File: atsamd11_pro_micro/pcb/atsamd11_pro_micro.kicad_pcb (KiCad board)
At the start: 2 copper layers, 33 x 17.8 mm, 24 parts, among them U1 MCP1700T-3302E/MB

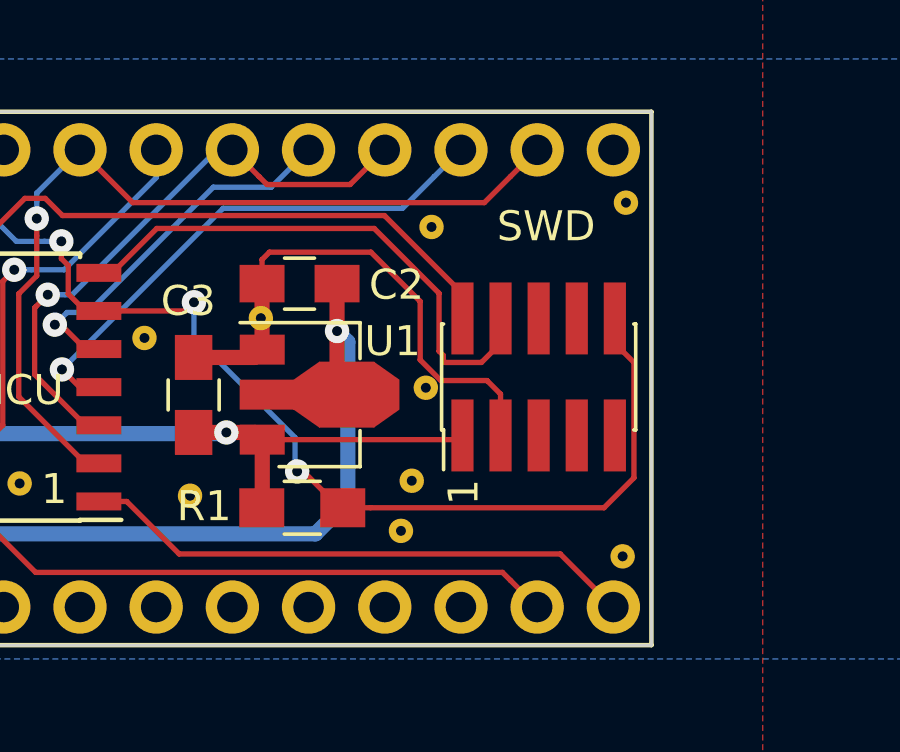
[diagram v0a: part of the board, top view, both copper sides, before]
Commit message: atsamd11_pro_micro: added missing SWCLK pullup
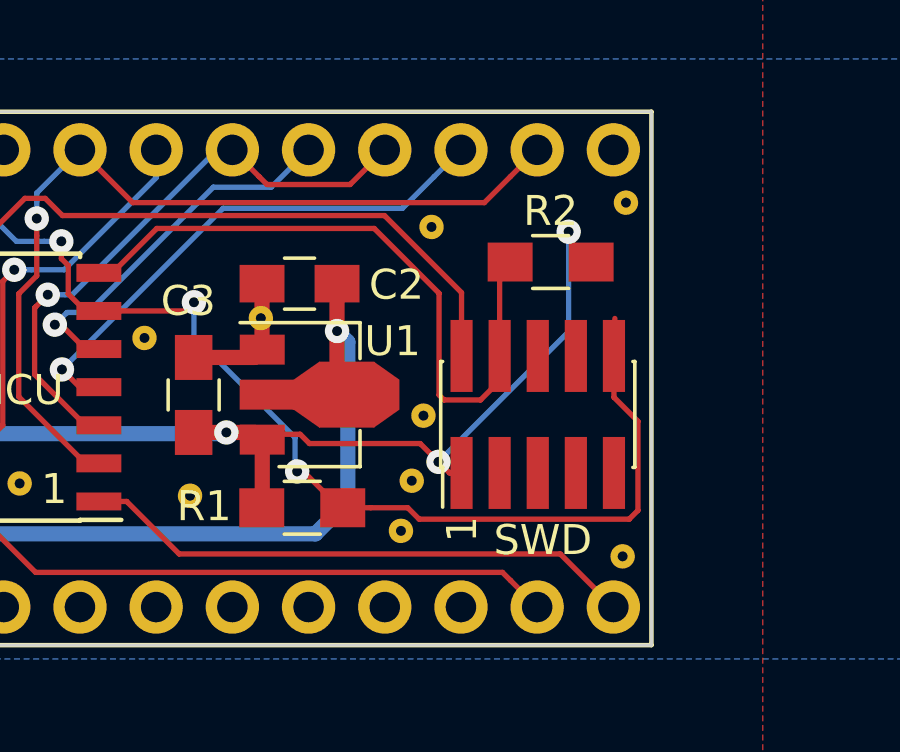
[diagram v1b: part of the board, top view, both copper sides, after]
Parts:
- added R2: 1k, Resistors_SMD:R_0805_HandSoldering, F.Cu at (157.9, 116.8)
- moved SWD 1.25 mm to (157.5, 121.8)
- moved staple_single15 0.93 mm to (153.7, 121.9)
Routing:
- net GND: track 23.5 -> 10.2 mm
- net 3V3: track 34.4 -> 45.7 mm, vias 2 -> 4
- net SWCLK: track 18.2 -> 22.7 mm
- net SWDIO: track 20.7 -> 21.9 mm
- net mcu_RESET: track 37.0 -> 37.7 mm
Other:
- board text added: "atsamd11 breakout board r2 Copyright 2017 Google Inc Designed by Phillip Pearson github.com/google/ myelin-acorn-electron-hardware"
- board text removed: "atsamd11 breakout board Copyright 2017 Google Inc Designed by Phillip Pearson github.com/google/ myelin-acorn-electron-hardware"

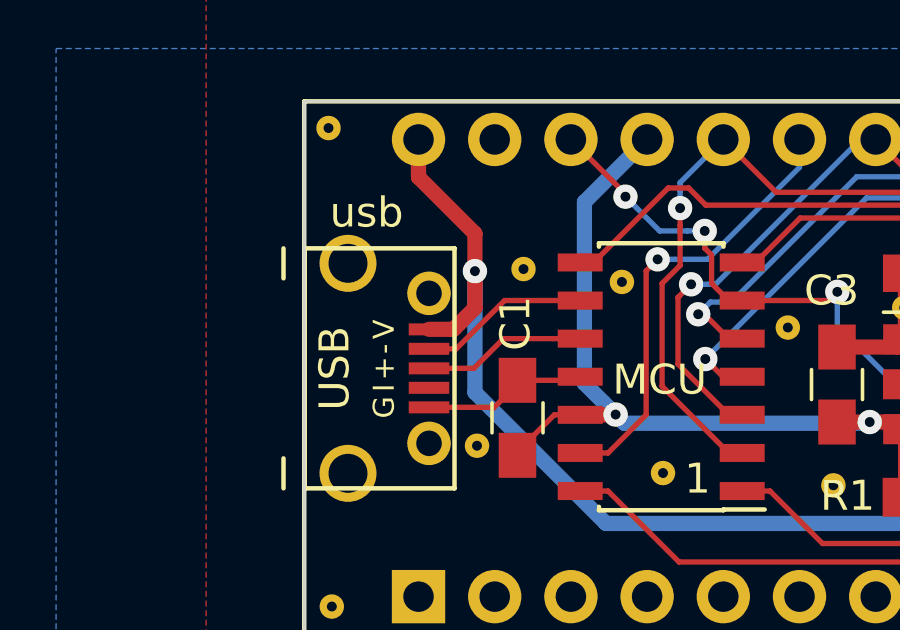
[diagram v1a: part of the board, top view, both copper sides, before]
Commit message: atsamd11_pro_micro tested out well
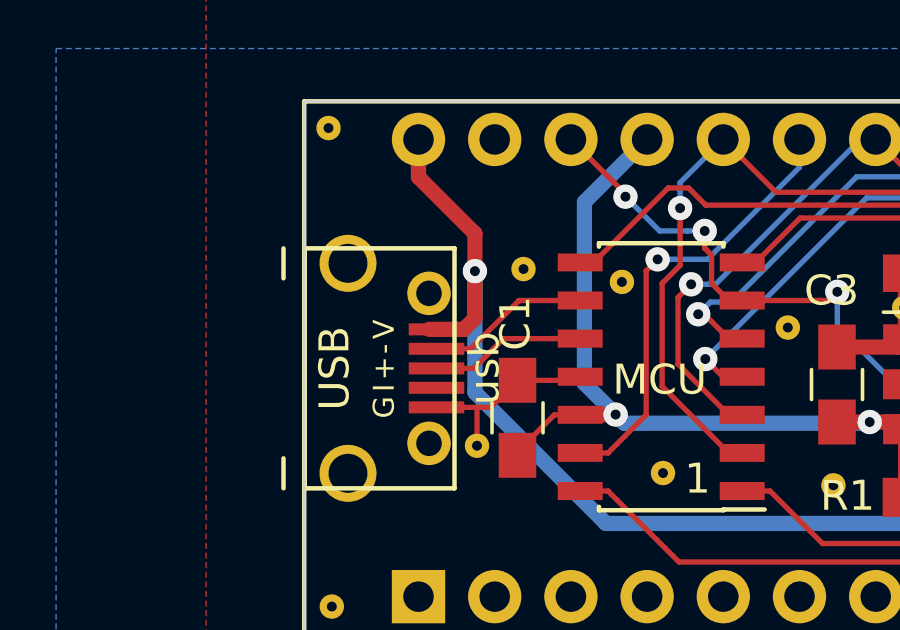
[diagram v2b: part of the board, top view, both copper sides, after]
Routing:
- net GND: track 10.2 -> 11.3 mm
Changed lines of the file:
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@@
     (links 56)
     (no_connects 0)
-    (area 128.219999 111.709999 161.340001 129.590001)
+    (area 120 105 170.000001 135.000001)
     (thickness 1.6)
     (drawings 7)
@@
     )
   )
-  (module myelin-kicad:micro_usb_b_smd_molex (layer F.Cu)
-    (at 130.28 120.66 270)
-    (descr "Molex SD-105017-001 bottom mount micro USB socket")
-    (fp_text reference USB (at 0 1 270) (layer F.SilkS)
-      (effects (font (size 1 1) (thickness 0.15)))
-    )
-    (fp_text value usb (at -5.19 -0.07 360) (layer F.SilkS)
-      (effects (font (size 1 1) (thickness 0.15)))
-    )
-    (fp_line (start -4 -3) (end 4 -3) (layer F.SilkS) (width 0.15))
-    (fp_line (start -4 -3) (end -4 2) (layer F.SilkS) (width 0.15))
-    (fp_line (start -4 2) (end 4 2) (layer F.SilkS) (width 0.15))
-    (fp_line (start 4 -3) (end 4 2) (layer F.SilkS) (width 0.15))
-    (fp_line (start -4 2.7) (end -3 2.7) (layer F.SilkS) (width 0.15))
-    (fp_line (start 3 2.7) (end 4 2.7) (layer F.SilkS) (width 0.15))
-    (fp_text user V (at -1.3 -0.65 270) (layer F.SilkS)
-      (effects (font (size 0.7 0.7) (thickness 0.15)))
-    )
-    (fp_text user - (at -0.65 -0.65 270) (layer F.SilkS)
-      (effects (font (size 0.7 0.7) (thickness 0.15)))
-    )
-    (fp_text user + (at 0 -0.65 270) (layer F.SilkS)
-      (effects (font (size 0.7 0.7) (thickness 0.15)))
-    )
-    (fp_text user I (at 0.65 -0.65 270) (layer F.SilkS)
-      (effects (font (size 0.7 0.7) (thickness 0.15)))
-    )
-    (fp_text user G (at 1.3 -0.65 270) (layer F.SilkS)
-      (effects (font (size 0.7 0.7) (thickness 0.15)))
-    )
-    (pad 1 smd rect (at -1.3 -2.15 270) (size 0.4 1.35) (layers F.Cu F.Paste F.Mask)
-      (net 2 5V))
-    (pad 2 smd rect (at -0.65 -2.15 270) (size 0.4 1.35) (layers F.Cu F.Paste F.Mask)
-      (net 12 USBDM))
-    (pad 3 smd rect (at 0 -2.15 270) (size 0.4 1.35) (layers F.Cu F.Paste F.Mask)
-      (net 13 USBDP))
-    (pad 4 smd rect (at 0.65 -2.15 270) (size 0.4 1.35) (layers F.Cu F.Paste F.Mask)
-      (net 18 USB_ID))
-    (pad 5 smd rect (at 1.3 -2.15 270) (size 0.4 1.35) (layers F.Cu F.Paste F.Mask)
-      (net 1 GND))
-    (pad P0 thru_hole circle (at -2.5 -2.15 270) (size 1.45 1.45) (drill 0.85) (layers *.Cu *.Mask))
-    (pad P1 thru_hole circle (at 2.5 -2.15 270) (size 1.45 1.45) (drill 0.85) (layers *.Cu *.Mask))
-    (pad M0 thru_hole circle (at -3.5 0.55 270) (size 1.9 1.9) (drill 1.3) (layers *.Cu *.Mask))
-    (pad M1 thru_hole circle (at 3.5 0.55 270) (size 1.9 1.9) (drill 1.3) (layers *.Cu *.Mask))
-  )
   (module myelin-kicad:via_single (layer F.Cu)
     (at 129.19 128.6)
@@
     )
   )
+  (module myelin-kicad:micro_usb_b_smd_molex (layer F.Cu)
+    (at 130.28 120.66 270)
+    (descr "Molex SD-105017-001 bottom mount micro USB socket")
+    (fp_text reference USB (at 0 1 270) (layer F.SilkS)
+      (effects (font (size 1 1) (thickness 0.15)))
+    )
+    (fp_text value usb (at 0 -4 270) (layer F.SilkS)
+      (effects (font (size 1 1) (thickness 0.15)))
+    )
+    (fp_line (start -4 -3) (end 4 -3) (layer F.SilkS) (width 0.15))
+    (fp_line (start -4 -3) (end -4 2) (layer F.SilkS) (width 0.15))
+    (fp_line (start -4 2) (end 4 2) (layer F.SilkS) (width 0.15))
+    (fp_line (start 4 -3) (end 4 2) (layer F.SilkS) (width 0.15))
+    (fp_line (start -4 2.7) (end -3 2.7) (layer F.SilkS) (width 0.15))
+    (fp_line (start 3 2.7) (end 4 2.7) (layer F.SilkS) (width 0.15))
+    (fp_text user V (at -1.3 -0.65 270) (layer F.SilkS)
+      (effects (font (size 0.7 0.7) (thickness 0.15)))
+    )
+    (fp_text user - (at -0.65 -0.65 270) (layer F.SilkS)
+      (effects (font (size 0.7 0.7) (thickness 0.15)))
+    )
+    (fp_text user + (at 0 -0.65 270) (layer F.SilkS)
+      (effects (font (size 0.7 0.7) (thickness 0.15)))
+    )
+    (fp_text user I (at 0.65 -0.65 270) (layer F.SilkS)
+      (effects (font (size 0.7 0.7) (thickness 0.15)))
+    )
+    (fp_text user G (at 1.3 -0.65 270) (layer F.SilkS)
+      (effects (font (size 0.7 0.7) (thickness 0.15)))
+    )
+    (pad 1 smd rect (at -1.3 -2.4 270) (size 0.4 1.85) (layers F.Cu F.Paste F.Mask)
+      (net 2 5V))
+    (pad 2 smd rect (at -0.65 -2.4 270) (size 0.4 1.85) (layers F.Cu F.Paste F.Mask)
+      (net 12 USBDM))
+    (pad 3 smd rect (at 0 -2.4 270) (size 0.4 1.85) (layers F.Cu F.Paste F.Mask)
+      (net 13 USBDP))
+    (pad 4 smd rect (at 0.65 -2.4 270) (size 0.4 1.85) (layers F.Cu F.Paste F.Mask)
+      (net 18 USB_ID))
+    (pad 5 smd rect (at 1.3 -2.4 270) (size 0.4 1.85) (layers F.Cu F.Paste F.Mask)
+      (net 1 GND))
+    (pad P0 thru_hole circle (at -2.5 -2.15 270) (size 1.45 1.45) (drill 0.85) (layers *.Cu *.Mask))
+    (pad P1 thru_hole circle (at 2.5 -2.15 270) (size 1.45 1.45) (drill 0.85) (layers *.Cu *.Mask))
+    (pad M0 thru_hole circle (at -3.5 0.55 270) (size 1.9 1.9) (drill 1.3) (layers *.Cu *.Mask))
+    (pad M1 thru_hole circle (at 3.5 0.55 270) (size 1.9 1.9) (drill 1.3) (layers *.Cu *.Mask))
+  )
   (gr_text 1 (at 154.98 125.68 90) (layer F.SilkS)
     (effects (font (size 1 1) (thickness 0.2)))
@@
   (gr_line (start 161.29 111.76) (end 161.29 129.54) (layer Edge.Cuts) (width 0.1))
   (gr_line (start 128.27 111.76) (end 161.29 111.76) (layer Edge.Cuts) (width 0.1))
+  (segment (start 132.43 121.96) (end 134.01 121.96) (width 0.1778) (layer F.Cu) (net 1))
+  (segment (start 134.01 121.96) (end 134.48 121.96) (width 0.1778) (layer F.Cu) (net 1))
+  (segment (start 134.03 123.24) (end 134.03 121.98) (width 0.1778) (layer F.Cu) (net 1))
+  (segment (start 134.03 121.98) (end 134.01 121.96) (width 0.1778) (layer F.Cu) (net 1))
+  (segment (start 134.48 121.96) (end 135.38 121.06) (width 0.1778) (layer F.Cu) (net 1))
   (segment (start 146.03 119.95) (end 148.0565 119.95) (width 0.508) (layer F.Cu) (net 1))
   (segment (start 148.0565 119.95) (end 148.3165 119.69) (width 0.508) (layer F.Cu) (net 1))
@@
   (segment (start 135.38 121.06) (end 137.35 121.06) (width 0.1778) (layer F.Cu) (net 1))
   (segment (start 137.35 121.06) (end 137.47 120.94) (width 0.1778) (layer F.Cu) (net 1))
-  (segment (start 132.43 121.96) (end 134.48 121.96) (width 0.1778) (layer F.Cu) (net 1))
-  (segment (start 134.48 121.96) (end 134.5078 121.9878) (width 0.1778) (layer F.Cu) (net 1))
-  (segment (start 134.5078 121.9878) (end 134.5772 121.9878) (width 0.1778) (layer F.Cu) (net 1))
-  (segment (start 134.5772 121.9878) (end 135.38 121.185) (width 0.1778) (layer F.Cu) (net 1))
-  (segment (start 135.38 121.185) (end 135.38 121.06) (width 0.1778) (layer F.Cu) (net 1))
+  (segment (start 133.96 117.42) (end 133.96 118.99) (width 0.508) (layer F.Cu) (net 2))
+  (segment (start 133.96 118.99) (end 133.59 119.36) (width 0.508) (layer F.Cu) (net 2))
+  (segment (start 133.59 119.36) (end 132.43 119.36) (width 0.508) (layer F.Cu) (net 2))
   (segment (start 150.81 119.07) (end 151.17 119.43) (width 0.508) (layer B.Cu) (net 2))
   (segment (start 151.17 119.43) (end 151.17 124.75) (width 0.508) (layer B.Cu) (net 2))
@@
   (segment (start 133.96 121.46) (end 133.96 117.42) (width 0.508) (layer B.Cu) (net 2))
   (segment (start 133.96 116.167235) (end 133.96 117.42) (width 0.508) (layer F.Cu) (net 2))
-  (segment (start 133.96 117.42) (end 133.96 118.65) (width 0.508) (layer F.Cu) (net 2))
   (via (at 133.96 117.42) (size 0.8128) (drill 0.3302) (layers F.Cu B.Cu) (net 2))
   (segment (start 132.08 113.03) (end 132.08 114.287235) (width 0.508) (layer F.Cu) (net 2))
   (segment (start 132.08 114.287235) (end 133.96 116.167235) (width 0.508) (layer F.Cu) (net 2))
-  (segment (start 133.96 118.65) (end 133.25 119.36) (width 0.508) (layer F.Cu) (net 2))
-  (segment (start 133.25 119.36) (end 132.43 119.36) (width 0.508) (layer F.Cu) (net 2))
   (segment (start 150.81 119.07) (end 150.81 120.87) (width 0.508) (layer F.Cu) (net 2))
   (segment (start 150.81 117.49) (end 150.81 119.07) (width 0.508) (layer F.Cu) (net 2))
@@
   (segment (start 141.656192 115.22) (end 152.39 115.22) (width 0.1778) (layer F.Cu) (net 11))
   (segment (start 154.96 117.79) (end 154.96 119.9) (width 0.1778) (layer F.Cu) (net 11))
-  (segment (start 133.336396 120.01) (end 133.2828 120.01) (width 0.1778) (layer F.Cu) (net 12))
-  (segment (start 134.946396 118.4) (end 133.336396 120.01) (width 0.1778) (layer F.Cu) (net 12))
-  (segment (start 137.47 118.4) (end 134.946396 118.4) (width 0.1778) (layer F.Cu) (net 12))
+  (segment (start 137.47 118.4) (end 135.43 118.4) (width 0.1778) (layer F.Cu) (net 12))
+  (segment (start 135.43 118.4) (end 133.82 120.01) (width 0.1778) (layer F.Cu) (net 12))
+  (segment (start 133.82 120.01) (end 133.2828 120.01) (width 0.1778) (layer F.Cu) (net 12))
   (segment (start 133.2828 120.01) (end 132.43 120.01) (width 0.1778) (layer F.Cu) (net 12))
   (segment (start 132.43 120.66) (end 133.924938 120.66) (width 0.1778) (layer F.Cu) (net 13))
